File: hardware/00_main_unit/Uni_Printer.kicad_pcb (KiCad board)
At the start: 4 copper layers, 81 x 127.5 mm, 181 parts, among them IC1 MAX17503ATP+, IC10 ITS4141NHUMA1, IC11 ITS4141NHUMA1, IC2 AM26C31CD, IC3 74HC14D, IC4 TLV1117-33, IC5 LAN8742A, IC6 ITS4141NHUMA1, IC7 ITS4141NHUMA1, IC8 ITS4141NHUMA1, IC9 ITS4141NHUMA1, J1 Conn_01x10, J10 USB B connector, J11 LMJ1998824110DL1T39J, J12 RJ45, J13 Conn_01x04_Male, J14 Conn_02x13_Odd_Even, J15 Conn_01x06_Male, J2 Conn_01x10, J3 Conn_01x10, J4 Conn_01x10, J5 FIDUCIAL, J6 FIDUCIAL, J7 Conn_01x10, J8 Conn_01x10, J9 RJ45, SW2 SW_Push, SW3 SW_Push, U1 STM32H743VIT6, U3 TLE9251VSJ, U5 ST1480ACDR, U6 ST1480ACDR, U7 ST1480ACDR, U8 ST1480ACDR, U9 ST1480ACDR, Y1 ABM7-25.000MHZ-D2Y-T, Y2 ABM7-25.000MHZ-D2Y-T

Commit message: Fixes before ordering PCB
Signed-off-by: Jarosław Karwik <jaroslaw.karwik@gmail.com>
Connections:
- IC1 pad 10: (no net) -> unconnected-(IC1-Pad10)
- IC1 pad 11: (no net) -> unconnected-(IC1-Pad11)
- IC1 pad 6: (no net) -> unconnected-(IC1-Pad6)
- IC1 pad 8: (no net) -> unconnected-(IC1-Pad8)
- IC5 pad 10: (no net) -> unconnected-(IC5-Pad10)
- J15 pad 2: (no net) -> unconnected-(J15-Pad2)
- J15 pad 3: (no net) -> unconnected-(J15-Pad3)
- J15 pad 6: (no net) -> unconnected-(J15-Pad6)
- J7 pad 10: (no net) -> /Connectors/DIR1.B
- J7 pad 7: (no net) -> /Connectors/STEP1.A
- J7 pad 8: (no net) -> /Connectors/STEP1.B
- J7 pad 9: (no net) -> /Connectors/DIR1.A
- J8 pad 10: (no net) -> /Connectors/DIR2.B
- J8 pad 7: (no net) -> /Connectors/STEP2.A
- J8 pad 8: (no net) -> /Connectors/STEP2.B
- J8 pad 9: (no net) -> /Connectors/DIR2.A
- RN11 pad 3: (no net) -> unconnected-(RN11-Pad3)
- RN11 pad 4: (no net) -> unconnected-(RN11-Pad4)
- RN11 pad 5: (no net) -> unconnected-(RN11-Pad5)
- RN11 pad 6: (no net) -> unconnected-(RN11-Pad6)
- RN12 pad 3: (no net) -> unconnected-(RN12-Pad3)
- RN12 pad 4: (no net) -> unconnected-(RN12-Pad4)
- RN4 pad 1: (no net) -> unconnected-(RN4-Pad1)
- RN4 pad 2: (no net) -> unconnected-(RN4-Pad2)
- RN4 pad 7: (no net) -> unconnected-(RN4-Pad7)
- RN4 pad 8: (no net) -> unconnected-(RN4-Pad8)
- RN5 pad 4: (no net) -> unconnected-(RN5-Pad4)
- RN5 pad 5: (no net) -> unconnected-(RN5-Pad5)
- RN6 pad 4: (no net) -> unconnected-(RN6-Pad4)
- RN6 pad 5: (no net) -> unconnected-(RN6-Pad5)
- RN7 pad 4: (no net) -> unconnected-(RN7-Pad4)
- RN7 pad 5: (no net) -> unconnected-(RN7-Pad5)
- RN8 pad 1: (no net) -> unconnected-(RN8-Pad1)
- RN8 pad 2: (no net) -> unconnected-(RN8-Pad2)
- RN8 pad 7: (no net) -> unconnected-(RN8-Pad7)
- RN8 pad 8: (no net) -> unconnected-(RN8-Pad8)
- U1 pad 17: (no net) -> unconnected-(U1-Pad17)
- U1 pad 2: (no net) -> unconnected-(U1-Pad2)
- U1 pad 20: (no net) -> unconnected-(U1-Pad20)
- U1 pad 22: (no net) -> unconnected-(U1-Pad22)
- U1 pad 36: (no net) -> unconnected-(U1-Pad36)
- U1 pad 38: (no net) -> /IN_CPU2
- U1 pad 43: (no net) -> unconnected-(U1-Pad43)
- U1 pad 46: (no net) -> unconnected-(U1-Pad46)
- U1 pad 54: (no net) -> unconnected-(U1-Pad54)
- U1 pad 60: (no net) -> unconnected-(U1-Pad60)
- U1 pad 61: (no net) -> unconnected-(U1-Pad61)
- U1 pad 62: (no net) -> unconnected-(U1-Pad62)
- U1 pad 7: (no net) -> unconnected-(U1-Pad7)
- U1 pad 78: (no net) -> unconnected-(U1-Pad78)
- U1 pad 79: (no net) -> unconnected-(U1-Pad79)
- U1 pad 8: (no net) -> unconnected-(U1-Pad8)
- U1 pad 80: (no net) -> unconnected-(U1-Pad80)
- U1 pad 83: (no net) -> unconnected-(U1-Pad83)
- U1 pad 9: (no net) -> unconnected-(U1-Pad9)
- U1 pad 90: (no net) -> unconnected-(U1-Pad90)
- U1 pad 98: (no net) -> unconnected-(U1-Pad98)
- U5 pad 4: (no net) -> unconnected-(U5-Pad4)
- U6 pad 4: (no net) -> unconnected-(U6-Pad4)
- U7 pad 4: (no net) -> unconnected-(U7-Pad4)
- U8 pad 4: (no net) -> unconnected-(U8-Pad4)
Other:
- board text added: "IN1_S"
- board text added: "IN2_S"
- board text added: "IN3_S"
- board text added: "IN4_S"
- board text added: "IN5_S"
- board text added: "IN6_S"
- board text added: "IN7_S"
- board text added: "IN8_S"
- board text removed: "IN1"
- board text removed: "IN2"
- board text removed: "IN3"
- board text removed: "IN4"
- board text removed: "IN5"
- board text removed: "IN6"
- board text removed: "IN7"
- board text removed: "IN8"

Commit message: Fixes for new hw version
Signed-off-by: Jarosław Karwik <jaroslaw.karwik@gmail.com>
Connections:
- D7 pad 3: /AIN_IN_ADC6 -> /Digital Inputs/AIN_IN_CPU6
- D7 pad 6: /AIN_IN_ADC5 -> /Digital Inputs/AIN_IN_CPU5
- D8 pad 3: /AIN_IN_ADC8 -> /Digital Inputs/AIN_IN_CPU8
- D8 pad 6: /AIN_IN_ADC7 -> /Digital Inputs/AIN_IN_CPU7
- R27 pad 2: /AIN_IN_ADC5 -> /Digital Inputs/AIN_IN_CPU5
- R31 pad 2: /AIN_IN_ADC6 -> /Digital Inputs/AIN_IN_CPU6
- R35 pad 2: /AIN_IN_ADC7 -> /Digital Inputs/AIN_IN_CPU7
- R42 pad 2: /AIN_IN_ADC8 -> /Digital Inputs/AIN_IN_CPU8
- U1 pad 28: /AIN_IN_ADC5 -> /AIN_IN_CPU5
- U1 pad 29: /AIN_IN_ADC6 -> /AIN_IN_CPU6
- U1 pad 34: /AIN_IN_ADC7 -> /AIN_IN_CPU7
- U1 pad 35: /AIN_IN_ADC8 -> /AIN_IN_CPU8
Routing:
- net /Digital Inputs/AIN_IN_CPU8: track 0.00 -> 67.6 mm, vias 0 -> 2
- net /AIN_IN_ADC8: track 67.6 -> 0.00 mm, vias 2 -> 0
- net /Digital Inputs/AIN_IN_CPU7: track 0.00 -> 65.1 mm, vias 0 -> 2
- net /AIN_IN_ADC7: track 65.1 -> 0.00 mm, vias 2 -> 0
- net /Digital Inputs/AIN_IN_CPU6: track 0.00 -> 48.3 mm, vias 0 -> 2
- net /AIN_IN_ADC6: track 48.3 -> 0.00 mm, vias 2 -> 0
- net /Digital Inputs/AIN_IN_CPU5: track 0.00 -> 45.4 mm, vias 0 -> 2
- net /AIN_IN_ADC5: track 45.4 -> 0.00 mm, vias 2 -> 0
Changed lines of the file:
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@@
   (net 24 "/Processor/D-")
   (net 25 "Net-(D9-Pad2)")
-  (net 26 "/AIN_IN_ADC6")
-  (net 27 "/AIN_IN_ADC5")
-  (net 28 "/AIN_IN_ADC8")
-  (net 29 "/AIN_IN_ADC7")
+  (net 26 "/Digital Inputs/AIN_IN_CPU6")
+  (net 27 "/Digital Inputs/AIN_IN_CPU5")
+  (net 28 "/Digital Inputs/AIN_IN_CPU8")
+  (net 29 "/Digital Inputs/AIN_IN_CPU7")
   (net 30 "/OUT_STEP1")
   (net 31 "/Processor/D+")
@@
   (net 245 "unconnected-(U7-Pad4)")
   (net 246 "unconnected-(U8-Pad4)")
+  (net 247 "/AIN_IN_CPU5")
+  (net 248 "/AIN_IN_CPU6")
+  (net 249 "/AIN_IN_CPU7")
+  (net 250 "/AIN_IN_CPU8")
   (footprint "Buttons_Switches_SMD:SW_SPST_B3U-1000P" (layer "F.Cu")
     (at 100.4 98.1)
@@
       (net 157 "/Connectors/AIN_IN7") (pintype "passive"))
     (pad "2" smd roundrect (at 0.7875 0 180) (locked) (size 0.875 0.95) (layers "F.Cu" "F.Paste" "F.Mask") (roundrect_rratio 0.25)
-      (net 29 "/AIN_IN_ADC7") (pintype "passive"))
+      (net 29 "/Digital Inputs/AIN_IN_CPU7") (pintype "passive"))
     (model "${KISYS3DMOD}/Resistor_SMD.3dshapes/R_0603_1608Metric.wrl"
       (offset (xyz 0 0 0))
@@
       (net 155 "/Connectors/AIN_IN6") (pintype "passive"))
     (pad "2" smd roundrect (at 0.7875 0 180) (locked) (size 0.875 0.95) (layers "F.Cu" "F.Paste" "F.Mask") (roundrect_rratio 0.25)
-      (net 26 "/AIN_IN_ADC6") (pintype "passive"))
+      (net 26 "/Digital Inputs/AIN_IN_CPU6") (pintype "passive"))
     (model "${KISYS3DMOD}/Resistor_SMD.3dshapes/R_0603_1608Metric.wrl"
       (offset (xyz 0 0 0))
@@
       (net 138 "/Connectors/AIN_IN5") (pintype "passive"))
     (pad "2" smd roundrect (at 0.7875 0 180) (locked) (size 0.875 0.95) (layers "F.Cu" "F.Paste" "F.Mask") (roundrect_rratio 0.25)
-      (net 27 "/AIN_IN_ADC5") (pintype "passive"))
+      (net 27 "/Digital Inputs/AIN_IN_CPU5") (pintype "passive"))
     (model "${KISYS3DMOD}/Resistor_SMD.3dshapes/R_0603_1608Metric.wrl"
       (offset (xyz 0 0 0))
@@
     (fp_line (start 0.8 0.4) (end -0.8 0.4) (layer "F.Fab") (width 0.1))
     (pad "1" smd roundrect (at -0.7875 0 180) (locked) (size 0.875 0.95) (layers "F.Cu" "F.Paste" "F.Mask") (roundrect_rratio 0.25)
-      (net 78 "/Connectors/IN1"))
+      (net 78 "/Connectors/IN1") (pintype "passive"))
     (pad "2" smd roundrect (at 0.7875 0 180) (locked) (size 0.875 0.95) (layers "F.Cu" "F.Paste" "F.Mask") (roundrect_rratio 0.25)
-      (net 18 "/IN_CPU1"))
+      (net 18 "/IN_CPU1") (pintype "passive"))
     (model "${KISYS3DMOD}/Resistor_SMD.3dshapes/R_0603_1608Metric.wrl"
       (offset (xyz 0 0 0))
@@
       (net 1 "+3V3") (pinfunction "K") (pintype "passive"))
     (pad "3" smd rect (at -0.9 0.75 270) (locked) (size 0.6 0.6) (layers "F.Cu" "F.Paste" "F.Mask")
-      (net 26 "/AIN_IN_ADC6") (pinfunction "C") (pintype "passive"))
+      (net 26 "/Digital Inputs/AIN_IN_CPU6") (pinfunction "C") (pintype "passive"))
     (pad "4" smd rect (at 0.9 0.75 270) (locked) (size 0.6 0.6) (layers "F.Cu" "F.Paste" "F.Mask")
       (net 2 "GND") (pinfunction "A") (pintype "passive"))
@@
       (net 1 "+3V3") (pinfunction "K") (pintype "passive"))
     (pad "6" smd rect (at 0.9 -0.75 270) (locked) (size 0.6 0.6) (layers "F.Cu" "F.Paste" "F.Mask")
-      (net 27 "/AIN_IN_ADC5") (pinfunction "C") (pintype "passive"))
+      (net 27 "/Digital Inputs/AIN_IN_CPU5") (pinfunction "C") (pintype "passive"))
     (model "smd_trans/sot323-6.wrl"
       (offset (xyz 0 0 0))
@@
       (net 1 "+3V3") (pinfunction "K") (pintype "passive"))
     (pad "3" smd rect (at -0.9 0.75 180) (locked) (size 0.6 0.6) (layers "F.Cu" "F.Paste" "F.Mask")
-      (net 28 "/AIN_IN_ADC8") (pinfunction "C") (pintype "passive"))
+      (net 28 "/Digital Inputs/AIN_IN_CPU8") (pinfunction "C") (pintype "passive"))
     (pad "4" smd rect (at 0.9 0.75 180) (locked) (size 0.6 0.6) (layers "F.Cu" "F.Paste" "F.Mask")
       (net 2 "GND") (pinfunction "A") (pintype "passive"))
@@
       (net 1 "+3V3") (pinfunction "K") (pintype "passive"))
     (pad "6" smd rect (at 0.9 -0.75 180) (locked) (size 0.6 0.6) (layers "F.Cu" "F.Paste" "F.Mask")
-      (net 29 "/AIN_IN_ADC7") (pinfunction "C") (pintype "passive"))
+      (net 29 "/Digital Inputs/AIN_IN_CPU7") (pinfunction "C") (pintype "passive"))
     (model "smd_trans/sot323-6.wrl"
       (offset (xyz 0 0 0))
@@
       (net 93 "/Connectors/AIN_IN8") (pintype "passive"))
     (pad "2" smd roundrect (at 0.7875 0 180) (locked) (size 0.875 0.95) (layers "F.Cu" "F.Paste" "F.Mask") (roundrect_rratio 0.25)
-      (net 28 "/AIN_IN_ADC8") (pintype "passive"))
+      (net 28 "/Digital Inputs/AIN_IN_CPU8") (pintype "passive"))
     (model "${KISYS3DMOD}/Resistor_SMD.3dshapes/R_0603_1608Metric.wrl"
       (offset (xyz 0 0 0))
@@
       (net 1 "+3V3") (pinfunction "VDD") (pintype "power_in"))
     (pad "28" smd roundrect (at -5 7.675 90) (locked) (size 0.3 1.6) (layers "F.Cu" "F.Paste" "F.Mask") (roundrect_rratio 0.25)
-      (net 27 "/AIN_IN_ADC5") (pinfunction "PA4") (pintype "bidirectional"))
+      (net 247 "/AIN_IN_CPU5") (pinfunction "PA4") (pintype "bidirectional"))
     (pad "29" smd roundrect (at -4.5 7.675 90) (locked) (size 0.3 1.6) (layers "F.Cu" "F.Paste" "F.Mask") (roundrect_rratio 0.25)
-      (net 26 "/AIN_IN_ADC6") (pinfunction "PA5") (pintype "bidirectional"))
+      (net 248 "/AIN_IN_CPU6") (pinfunction "PA5") (pintype "bidirectional"))
     (pad "30" smd roundrect (at -4 7.675 90) (locked) (size 0.3 1.6) (layers "F.Cu" "F.Paste" "F.Mask") (roundrect_rratio 0.25)
       (net 169 "/ENC1.CH1") (pinfunction "PA6") (pintype "bidirectional"))
@@
       (net 53 "/Ethernet/ENET_RXD1") (pinfunction "PC5") (pintype "bidirectional"))
     (pad "34" smd roundrect (at -2 7.675 90) (locked) (size 0.3 1.6) (layers "F.Cu" "F.Paste" "F.Mask") (roundrect_rratio 0.25)
-      (net 29 "/AIN_IN_ADC7") (pinfunction "PB0") (pintype "bidirectional"))
+      (net 249 "/AIN_IN_CPU7") (pinfunction "PB0") (pintype "bidirectional"))
     (pad "35" smd roundrect (at -1.5 7.675 90) (locked) (size 0.3 1.6) (layers "F.Cu" "F.Paste" "F.Mask") (roundrect_rratio 0.25)
-      (net 28 "/AIN_IN_ADC8") (pinfunction "PB1") (pintype "bidirectional"))
+      (net 250 "/AIN_IN_CPU8") (pinfunction "PB1") (pintype "bidirectional"))
     (pad "36" smd roundrect (at -1 7.675 90) (locked) (size 0.3 1.6) (layers "F.Cu" "F.Paste" "F.Mask") (roundrect_rratio 0.25)
       (net 229 "unconnected-(U1-Pad36)") (pinfunction "PB2") (pintype "bidirectional+no_connect"))
@@
     (fp_line (start -2.3 1.25) (end 2.3 1.25) (layer "B.CrtYd") (width 0.05))
     (pad "1" smd custom (at -1.3 0 180) (locked) (size 1 0.5) (layers "B.Cu" "B.Mask")
-      (net 115 "Net-(JP14-Pad1)") (pinfunction "A") (zone_connect 2)
+      (net 115 "Net-(JP14-Pad1)") (pinfunction "A") (pintype "passive") (zone_connect 2)
       (options (clearance outline) (anchor rect))
       (primitives
@@
       ))
     (pad "2" smd rect (at 0 0 180) (locked) (size 1 1.5) (layers "B.Cu" "B.Mask")
-      (net 155 "/Connectors/AIN_IN6") (pinfunction "C"))
+      (net 155 "/Connectors/AIN_IN6") (pinfunction "C") (pintype "input"))
     (pad "3" smd custom (at 1.3 0 180) (locked) (size 1 0.5) (layers "B.Cu" "B.Mask")
-      (net 116 "Net-(JP14-Pad3)") (pinfunction "B") (zone_connect 2)
+      (net 116 "Net-(JP14-Pad3)") (pinfunction "B") (pintype "passive") (zone_connect 2)
       (options (clearance outline) (anchor rect))
       (primitives

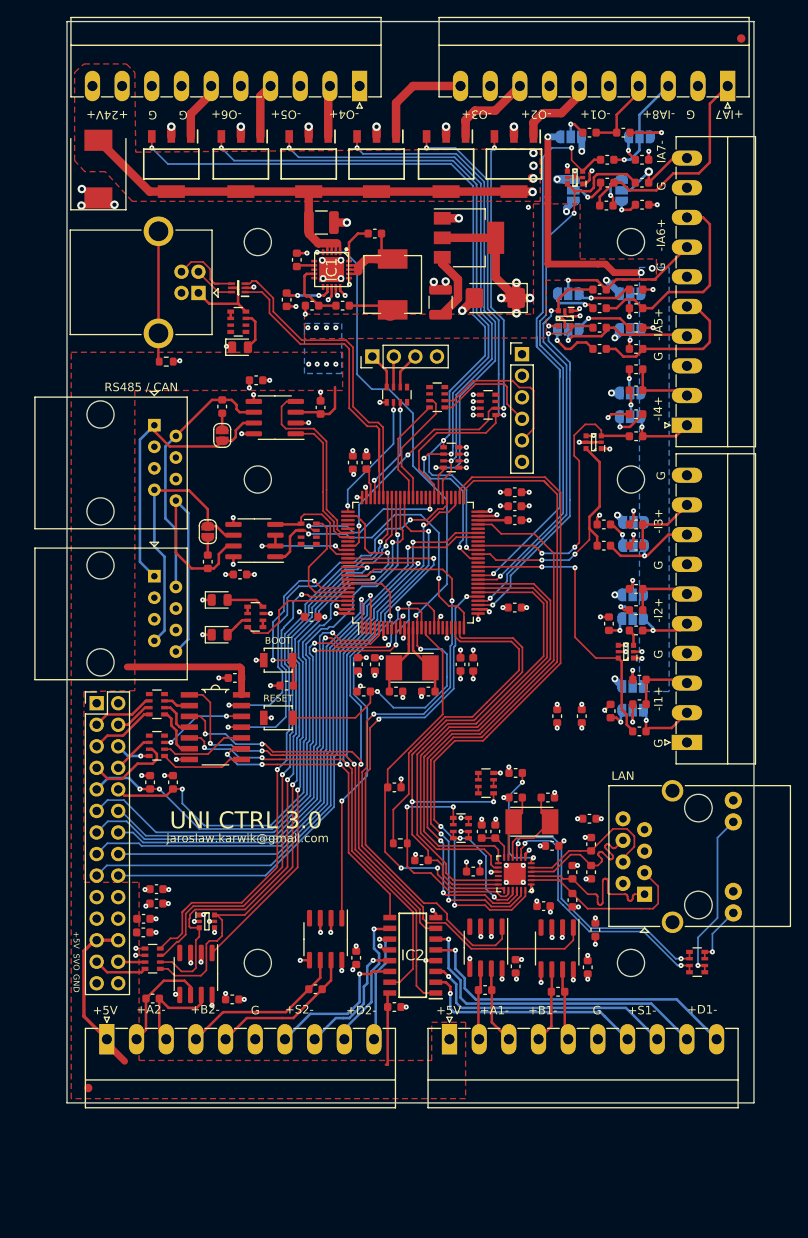
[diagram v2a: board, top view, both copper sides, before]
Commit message: Remote mode fixes
Signed-off-by: Jarosław Karwik <jaroslaw.karwik@gmail.com>
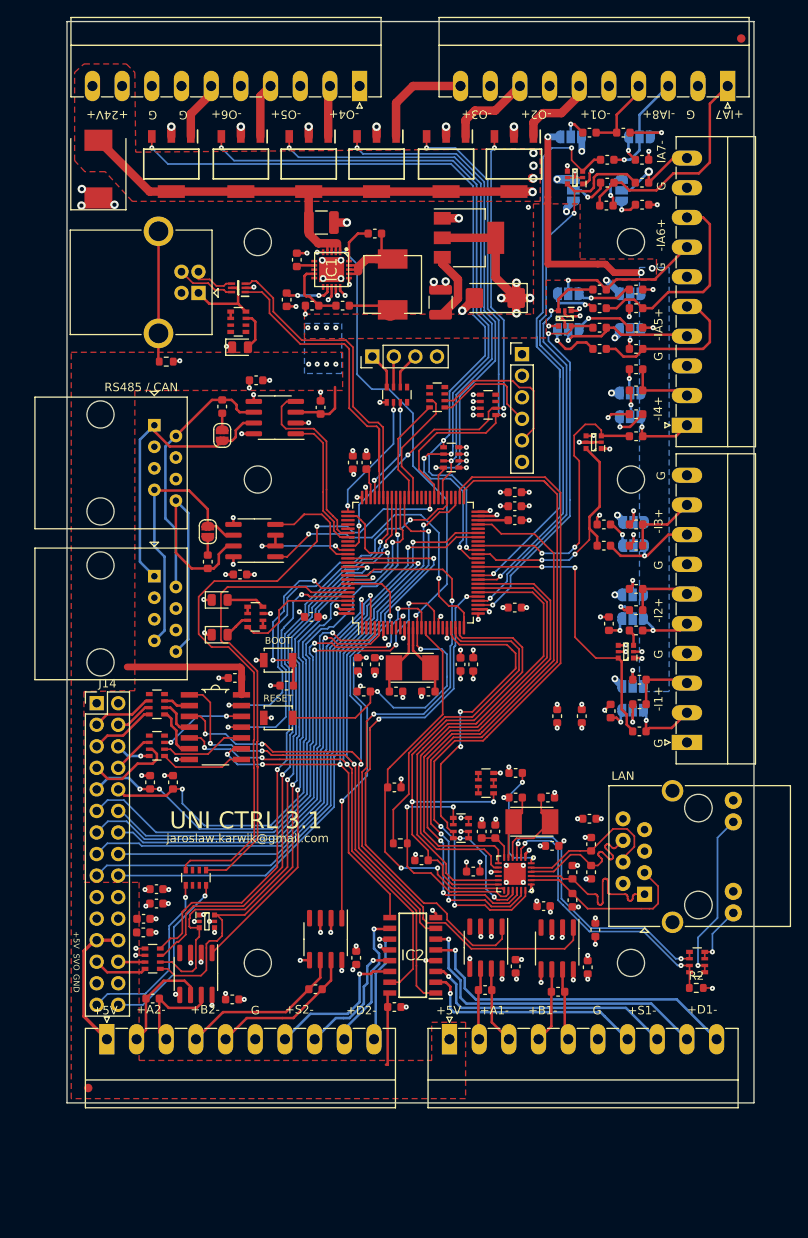
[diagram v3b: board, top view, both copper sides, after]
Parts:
- added R2: 12k1, Resistor_SMD:R_0603_1608Metric, F.Cu at (149.7, 129.9)
- J14: value Conn_02x13_Odd_Even -> Conn_02x15_Odd_Even; footprint Connector_PinHeader_2.54mm:PinHeader_2x14_P2.54mm_Vertical -> Connector_PinHeader_2.54mm:PinHeader_2x15_P2.54mm_Vertical
- moved RN4 42.7 mm to (90.7, 117.0), turned to 90 degrees
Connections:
- net /MID_IO1 renamed /MID_IO.IO1
- net /MID_IO2 renamed /MID_IO.IO2
- net /Power_supply/PWR_RESET renamed /Processor/NRST
- D7 pad 3: /Digital Inputs/AIN_IN_CPU6 -> /AIN_IN_ADC6
- D7 pad 6: /Digital Inputs/AIN_IN_CPU5 -> /AIN_IN_ADC5
- D8 pad 3: /Digital Inputs/AIN_IN_CPU8 -> /AIN_IN_ADC8
- D8 pad 6: /Digital Inputs/AIN_IN_CPU7 -> /AIN_IN_ADC7
- J10 pad 2: /USB.D+ -> /USB.D-
- J10 pad 3: /USB.D- -> /USB.D+
- R27 pad 2: /Digital Inputs/AIN_IN_CPU5 -> /AIN_IN_ADC5
- R31 pad 2: /Digital Inputs/AIN_IN_CPU6 -> /AIN_IN_ADC6
- R35 pad 2: /Digital Inputs/AIN_IN_CPU7 -> /AIN_IN_ADC7
- R42 pad 2: /Digital Inputs/AIN_IN_CPU8 -> /AIN_IN_ADC8
- RN4 pad 1: unconnected-(RN4-Pad1) -> Net-(J14-Pad29)
- RN4 pad 3: /Processor/LPTM1_IN1_PD12 -> unconnected-(RN4-Pad3)
- RN4 pad 4: /Processor/TIM16_CH1__PB8 -> Net-(J14-Pad30)
- RN4 pad 5: /RS485_RX -> /MID_IO.IO4_STEP4
- RN4 pad 6: /RS485_TX -> unconnected-(RN4-Pad6)
- RN4 pad 8: unconnected-(RN4-Pad8) -> /MID_IO.IO3_DIR4
- U1 pad 22: unconnected-(U1-Pad22) -> /Ethernet/ENET_RST
- U1 pad 28: /AIN_IN_CPU5 -> /AIN_IN_ADC5
- U1 pad 29: /AIN_IN_CPU6 -> /AIN_IN_ADC6
- U1 pad 34: /AIN_IN_CPU7 -> /AIN_IN_ADC7
- U1 pad 35: /AIN_IN_CPU8 -> /AIN_IN_ADC8
- U1 pad 59: /Processor/LPTM1_IN1_PD12 -> /MID_IO.IO3_DIR4
- U1 pad 95: /Processor/TIM16_CH1__PB8 -> /MID_IO.IO4_STEP4
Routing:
- net /MID_IO.IO3_DIR4: track 0.00 -> 76.9 mm, vias 0 -> 2
- net /Digital Inputs/AIN_IN_CPU8: track 67.6 -> 0.00 mm, vias 2 -> 0
- net /AIN_IN_ADC8: track 0.00 -> 67.6 mm, vias 0 -> 2
- net /Digital Inputs/AIN_IN_CPU7: track 65.1 -> 0.00 mm, vias 2 -> 0
- net /AIN_IN_ADC7: track 0.00 -> 65.1 mm, vias 0 -> 2
- net /MID_IO.IO4_STEP4: track 0.00 -> 54.3 mm
- net /Digital Inputs/AIN_IN_CPU6: track 48.3 -> 0.00 mm, vias 2 -> 0
- net /AIN_IN_ADC6: track 0.00 -> 48.3 mm, vias 0 -> 2
- net /Digital Inputs/AIN_IN_CPU5: track 45.4 -> 0.00 mm, vias 2 -> 0
- net /AIN_IN_ADC5: track 0.00 -> 45.4 mm, vias 0 -> 2
- net /Ethernet/ENET_RST: track 13.8 -> 49.8 mm, vias 2 -> 4
- net Net-(J14-Pad29): track 0.00 -> 21.0 mm, vias 0 -> 1
- net Net-(J14-Pad30): track 0.00 -> 20.1 mm, vias 0 -> 1
- net /Processor/LPTM1_IN1_PD12: track 18.3 -> 0.00 mm, vias 2 -> 0
- net /Processor/TIM16_CH1__PB8: track 14.1 -> 0.00 mm
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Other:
- board text added: "UNI CTRL 3.1"
- board text removed: "UNI CTRL 3.0"
